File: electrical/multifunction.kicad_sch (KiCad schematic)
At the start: 23 parts

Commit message: Interim check-in
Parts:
- removed AVIONICS_CTL_SW, CABIN_CTL_SW, PANEL_CTL_SW: ~, symbol Switch:SW_SPST
- removed SMOKE_SW: SW_Push, symbol Switch:SW_Push
- added CWS_SW, PILOT_PTT: SW_Push, symbol Switch:SW_Push
- added PITCH_SW: SW_SPDT, symbol flyerx:SW_SPDT
- added SMKP, SMKP2: DT2P, symbol Connector:Conn_01x02_Socket
- added SMKR, SMKR2: DT2R, symbol Connector:Conn_01x02_Pin
- added SMOKE_SW: ~, symbol Switch:SW_SPST
- added STKP: DTM8P, symbol Connector:Conn_01x08_Socket
- added STKR: DTM8R, symbol Connector:Conn_01x08_Pin
- renumbered LANDING_LT to LEFT_LT, TAXI_LT to RIGHT_LT
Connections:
- net CAN_HI_IN: now also PILOT_PTT.1, STKP.8 (Pin_8), STKR.8 (Pin_8)
- net GND: now also PITCH_SW.2 (B), STKR.1 (Pin_1); no longer FLAPS_DN_SW.2, FLAPS_UP_SW.2, LEFT_LT.2, LEVEL_SW.2, RIGHT_LT.2
- net LIGHTING_12V: now also AVIONICS_CTL_POT.1, CABIN_CTL_POT.1, PANEL_CTL_POT.1
- net FUEL_PUMP_ON: now reaches GAD27.P271_10 (DISCRETE_IN_2)
- net FUEL_PUMP_ON: no longer GAD27.P271_28 (PILOT_ROLL_TRIM_L)
- net SMOKE_LT_ON: now reaches GAD27.P271_11 (DISCRETE_IN_3)
- net SMOKE_LT_ON: now also SMOKE_LT_FS.2, STKR.5 (Pin_5)
- net Orange: now reaches FLAPS_UP_SW.1
- net Orange: now also STKP.2 (Pin_2); no longer GAD27.P271_18 (FLAP_UP_1_SWITCH/ABS_FLAP_POSITION_1)
- net Grey: now reaches FLAPS_DN_SW.1
- net Grey: now also STKP.3 (Pin_3); no longer GAD27.P271_19 (FLAP_DOWN_1_SWITCH/ABS_FLAP_POSITION_2)
- net at GAD27.P271_24 (PILOT_PITCH_TRIM_UP): now also PITCH_SW.3 (C)
- net at GAD27.P271_25 (PILOT_PITCH_TRIM_DN): now also PITCH_SW.1 (A)
- net Purple: now reaches LEVEL_SW.1
- net Purple: now also STKP.6 (Pin_6); no longer GAD27.P271_9 (DISCRETE_IN_1)
- net PITCH_TRIM_PWR: now reaches GAD27.P272_1 (PITCH_TRIM_POWER_IN)
- net PITCH_TRIM1: now reaches GAD27.P272_11 (PITCH_TRIM_OUT_1)
- net PITCH_TRIM2: now reaches GAD27.P272_12 (PITCH_TRIM_OUT_2)
- net at GAD27.P272_9 (ROLL_TRIM_OUT_1), SMOKE_LT_FS.1: now also SMKR.1 (Pin_1); no longer SMOKE.1 (+)
- net at GAD27.TB_7 (FLAP_POWER_OUT_1): now also SMKR2.1 (Pin_1); no longer FLAPS.1 (+)
- net at GAD27.TB_8 (FLAP_POWER_OUT_2): now also SMKR2.2 (Pin_2); no longer FLAPS.2 (-)
- net Brown: now reaches SMOKE_LT.1
- net Brown: now also STKP.5 (Pin_5); no longer SMOKE_LT_FS.2
- new net: GAD27.P272_10 (ROLL_TRIM_OUT_2), SMKR.2 (Pin_2)
- new net: FLAPS.1 (+), SMKP2.1 (Pin_1)
- new net: FLAPS.2 (-), SMKP2.2 (Pin_2)
- new net: SMKP.1 (Pin_1), SMOKE.1 (+)
- new net: SMKP.2 (Pin_2), SMOKE.2 (-)
- new net Black: CWS_SW.2, FLAPS_DN_SW.2, FLAPS_UP_SW.2, LEVEL_SW.2, PILOT_PTT.2, SMOKE_LT.2, SMOKE_SW.2 (B), STKP.1 (Pin_1)
- new net CWS_ON: STKR.7 (Pin_7)
- new net Earth: LEFT_LT.2, RIGHT_LT.2
- new net Pink: SMOKE_SW.1 (A), STKP.4 (Pin_4)
- new net Red: CWS_SW.1, STKP.7 (Pin_7)
- new net White/Green: GAD27.P271_28 (PILOT_ROLL_TRIM_L), STKR.4 (Pin_4)
- new net White/Grey: GAD27.P271_19 (FLAP_DOWN_1_SWITCH/ABS_FLAP_POSITION_2), STKR.3 (Pin_3)
- new net White/Orange: GAD27.P271_18 (FLAP_UP_1_SWITCH/ABS_FLAP_POSITION_1), STKR.2 (Pin_2)
- new net White/Purple: GAD27.P271_9 (DISCRETE_IN_1), STKR.6 (Pin_6)
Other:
- moved on the sheet: AVIONICS_CTL_POT, CABIN_CTL_POT, FLAPS, FLAPS_DN_SW, FLAPS_UP_SW, LANDING_SW, LEVEL_SW, PANEL_CTL_POT, SMOKE, SMOKE_LT, TAXI_SW, WAG_SW

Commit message: Updated from learnings from N78HR
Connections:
- net FUEL_PUMP_ON is gone; now on net SMOKE_LT_ON: GAD27.P271_10 (DISCRETE_IN_2)
- net SMOKE_LT_ON: no longer GAD27.P271_11 (DISCRETE_IN_3)
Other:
- note added: "Not sure if using the Roll Trim will work for smoke"

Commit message: Interim check-in
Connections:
- net PITCH_TRIM1 is gone; now on net CAN_HI_IN: GAD27.P272_11 (PITCH_TRIM_OUT_1)
- net PITCH_TRIM2 is gone; now on net CAN_LO_IN: GAD27.P272_12 (PITCH_TRIM_OUT_2)
- net CAN_HI_IN: now also GAD27.P272_9 (ROLL_TRIM_OUT_1), GAD27.TB_7 (FLAP_POWER_OUT_1), SMKR.1 (Pin_1), SMKR2.1 (Pin_1), SMOKE_LT_FS.1
- net CAN_LO_IN: now also GAD27.P272_10 (ROLL_TRIM_OUT_2), GAD27.TB_8 (FLAP_POWER_OUT_2), SMKR.2 (Pin_2), SMKR2.2 (Pin_2)
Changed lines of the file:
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@@
 	(wire
 		(pts
+			(xy 83.82 175.26) (xy 97.79 175.26)
+		)
+		(stroke
+			(width 0)
+			(type dash)
+		)
+	)
+	(wire
+		(pts
 			(xy 81.28 74.93) (xy 100.33 74.93)
 		)
@@
 		)
 	)
+	(label "White"
+		(at 81.28 217.17 0)
+		(effects
+			(font
+				(size 1.27 1.27)
+			)
+			(justify left bottom)
+		)
+	)
 	(label "White{slash}Yellow"
 		(at 134.62 71.12 180)
@@
 		)
 	)
+	(label "White"
+		(at 81.28 177.8 0)
+		(effects
+			(font
+				(size 1.27 1.27)
+			)
+			(justify left bottom)
+		)
+	)
 	(label "Grey"
 		(at 144.78 66.04 0)
@@
 		)
 	)
+	(label "White{slash}Blue"
+		(at 81.28 180.34 0)
+		(effects
+			(font
+				(size 1.27 1.27)
+			)
+			(justify left bottom)
+		)
+	)
 	(label "White{slash}Black"
 		(at 134.62 60.96 180)
@@
 		)
 	)
+	(label "White{slash}Blue"
+		(at 111.76 185.42 180)
+		(effects
+			(font
+				(size 1.27 1.27)
+			)
+			(justify right bottom)
+		)
+	)
+	(label "White"
+		(at 111.76 182.88 180)
+		(effects
+			(font
+				(size 1.27 1.27)
+			)
+			(justify right bottom)
+		)
+	)
+	(label "White"
+		(at 81.28 182.88 0)
+		(effects
+			(font
+				(size 1.27 1.27)
+			)
+			(justify left bottom)
+		)
+	)
+	(label "White"
+		(at 116.84 217.17 180)
+		(effects
+			(font
+				(size 1.27 1.27)
+			)
+			(justify right bottom)
+		)
+	)
 	(label "White{slash}Purple"
 		(at 134.62 73.66 180)
@@
 	)
 	(label "White{slash}Blue"
+		(at 81.28 219.71 0)
+		(effects
+			(font
+				(size 1.27 1.27)
+			)
+			(justify left bottom)
+		)
+	)
+	(label "White{slash}Blue"
+		(at 81.28 185.42 0)
+		(effects
+			(font
+				(size 1.27 1.27)
+			)
+			(justify left bottom)
+		)
+	)
+	(label "White{slash}Blue"
+		(at 116.84 219.71 180)
+		(effects
+			(font
+				(size 1.27 1.27)
+			)
+			(justify right bottom)
+		)
+	)
+	(label "White{slash}Blue"
 		(at 81.28 35.56 0)
 		(effects
@@
 		(dnp no)
 		(property "Reference" "LEFT_LT"
-			(at 91.44 210.82 0)
+			(at 116.078 211.582 0)
 			(effects
 				(font
@@
 		(dnp no)
 		(property "Reference" "RIGHT_LT"
-			(at 91.44 213.36 0)
+			(at 116.586 213.868 0)
 			(effects
 				(font
@@
 					(unit 1)
 				)
+			)
+		)
+	)
+	(symbol
+		(lib_id "power:GNDS")
+		(at 83.82 175.26 270)
+		(unit 1)
+		(exclude_from_sim no)
+		(in_bom yes)
+		(on_board yes)
+		(dnp no)
+		(fields_autoplaced yes)
+		(property "Reference" "#PWR053"
+			(at 77.47 175.26 0)
+			(effects
+				(font
+					(size 1.27 1.27)
+				)
+				(hide yes)
+			)
+		)
+		(property "Value" "GNDS"
+			(at 78.74 175.26 0)
+			(effects
+				(font
+					(size 1.27 1.27)
+				)
+				(hide yes)
+			)
+		)
+		(property "Footprint" ""
+			(at 83.82 175.26 0)
+			(effects
+				(font
+					(size 1.27 1.27)
+				)
+				(hide yes)
+			)
+		)
+		(property "Datasheet" ""
+			(at 83.82 175.26 0)
+			(effects
+				(font
+					(size 1.27 1.27)
+				)
+				(hide yes)
+			)
+		)
+		(property "Description" "Power symbol creates a global label with name \"GNDS\" , signal ground"
+			(at 83.82 175.26 0)
+			(effects
+				(font
+					(size 1.27 1.27)
+				)
+				(hide yes)
+			)
+		)
+		(pin "1"
+		)
+		(instances
+			(project "electrical"
+				(path "/e8ec215a-dbe2-4eba-a577-e50a0a128049/67540fe5-9b6d-4d8c-9d03-cde1487f48ae"
+					(reference "#PWR053")
+					(unit 1)
+				)

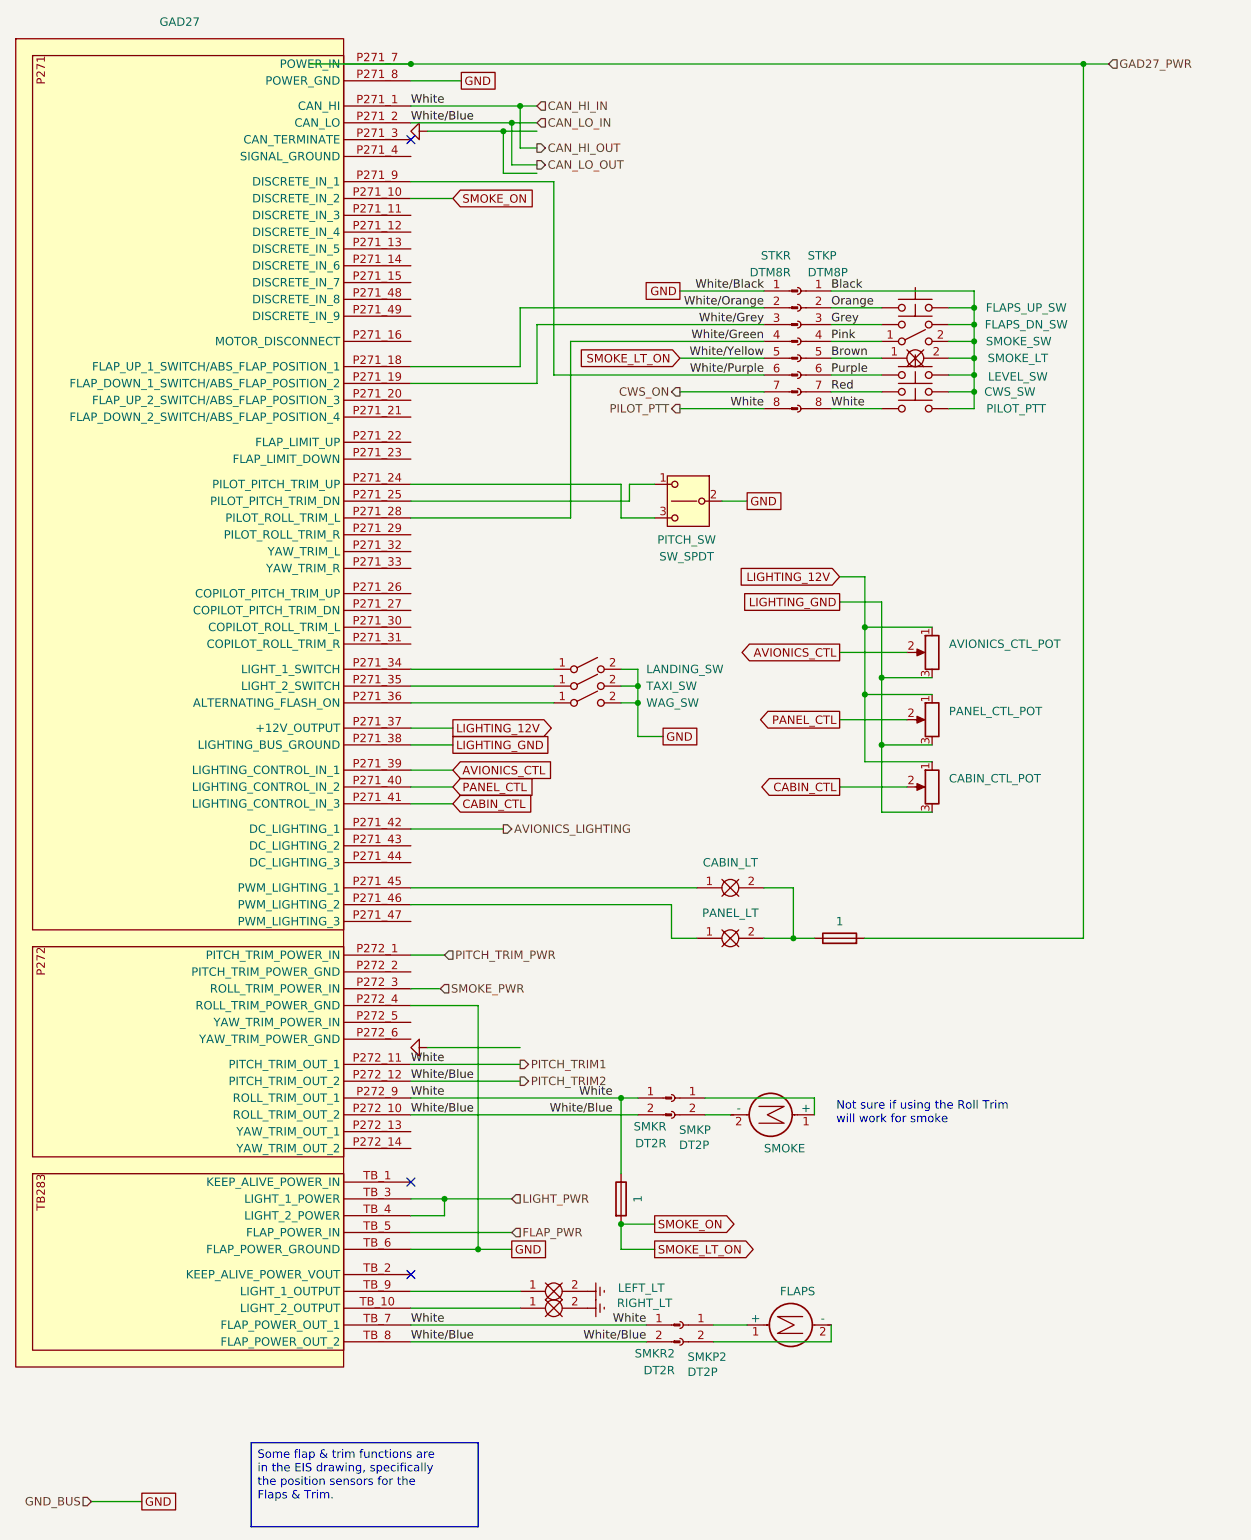
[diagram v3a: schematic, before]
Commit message: Went through and changed a lot from discussions and tradeoffs. Added GTX 330, rmemoved Connext from GDU and added to GPS 175 from GDL 52. Added relay for smoke and to not use GAD 27. Added Tach sensor for SureFly. Added carb heat. Added connectors to run panel disconnected.
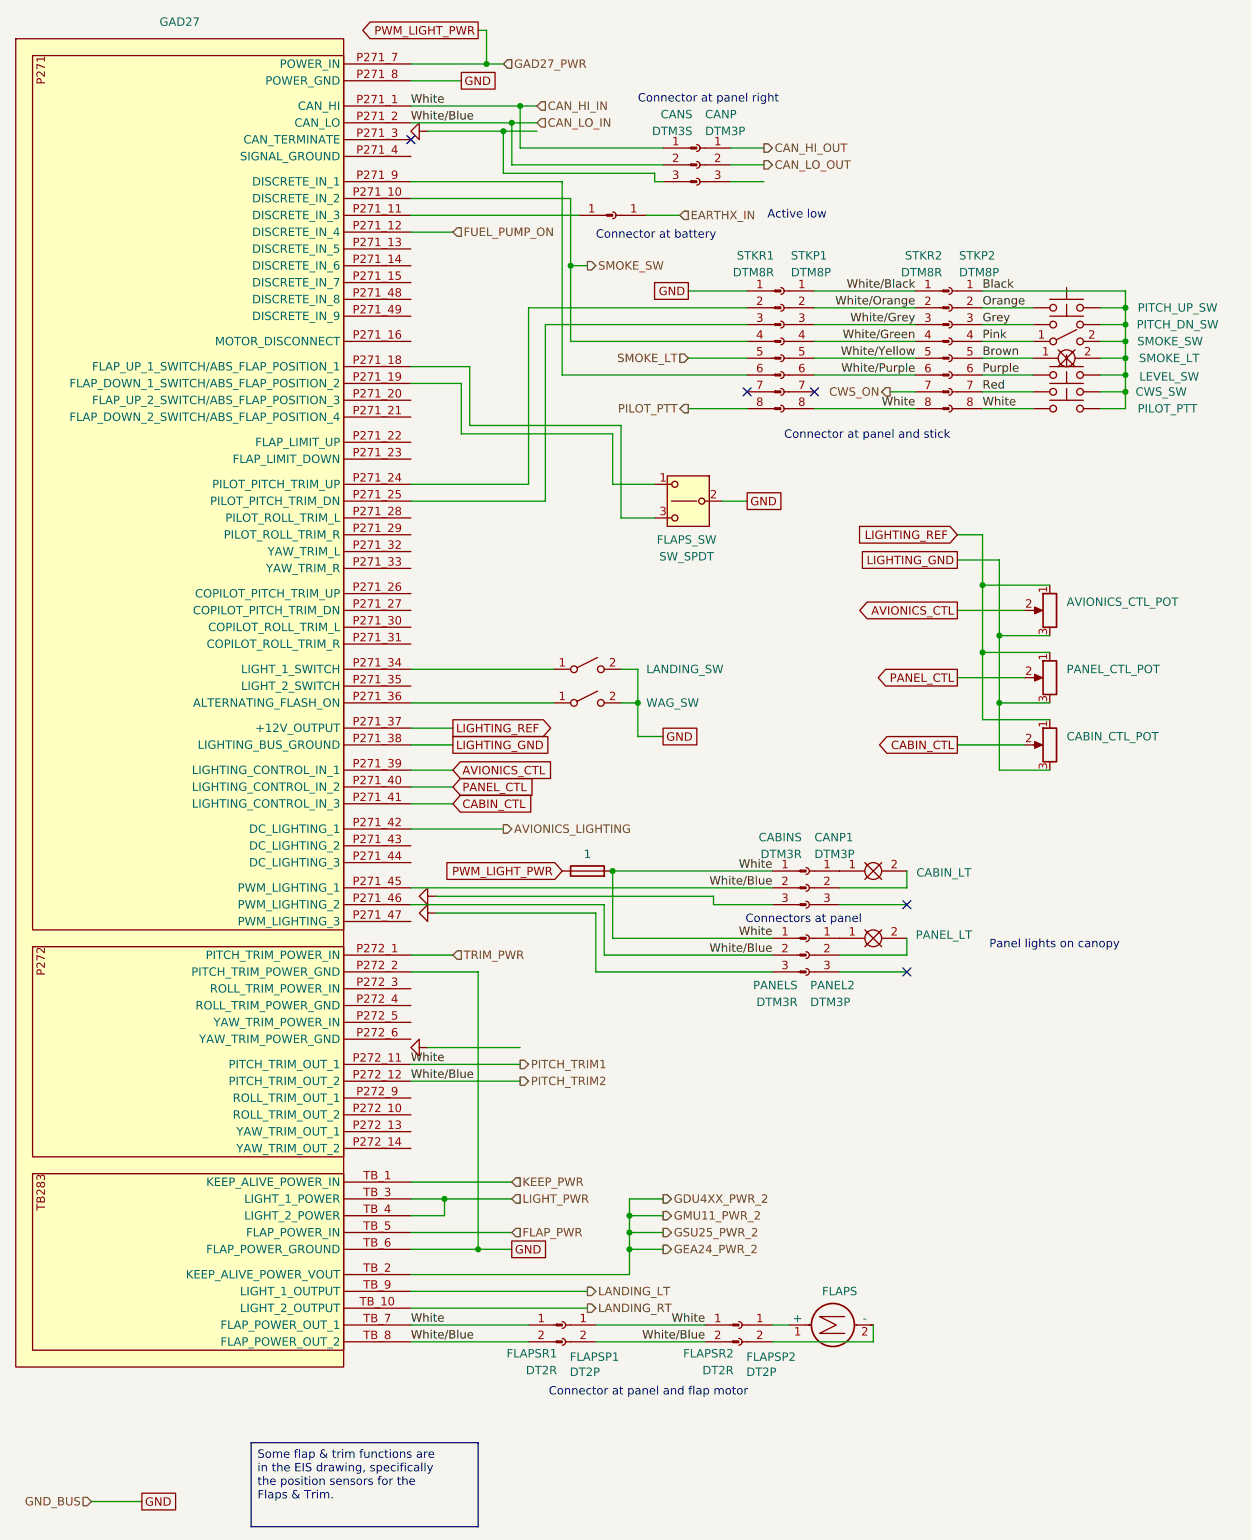
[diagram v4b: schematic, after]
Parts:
- removed LEFT_LT, RIGHT_LT: ~, symbol flyerx:Bulb
- removed SMKP: DT2P, symbol Connector:Conn_01x02_Socket
- removed SMKR: DT2R, symbol Connector:Conn_01x02_Pin
- removed SMOKE: Motor_DC, symbol Motor:Motor_DC
- removed SMOKE_LT_FS: 1, symbol Device:Fuse
- removed TAXI_SW: ~, symbol Switch:SW_SPST
- added CABINS, PANELS: DTM3R, symbol Connector:Conn_01x03_Pin
- added CANP, CANP1, PANEL2: DTM3P, symbol Connector:Conn_01x03_Socket
- added CANS: DTM3S, symbol Connector:Conn_01x03_Pin
- added EARTHXP: Conn_01x01_Pin, symbol Connector:Conn_01x01_Pin
- added EARTHXS: Conn_01x01_Socket, symbol Connector:Conn_01x01_Socket
- added FLAPSP1: DT2P, symbol Connector:Conn_01x02_Socket
- added FLAPSR1: DT2R, symbol Connector:Conn_01x02_Pin
- added STKP1: DTM8P, symbol Connector:Conn_01x08_Socket
- added STKR1: DTM8R, symbol Connector:Conn_01x08_Pin
- renumbered SMKP2 to FLAPSP2, SMKR2 to FLAPSR2, PITCH_SW to FLAPS_SW, FLAPS_DN_SW to PITCH_DN_SW, FLAPS_UP_SW to PITCH_UP_SW, STKP to STKP2, STKR to STKR2
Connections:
- net CAN_HI_IN: now also PANEL_LT_FS.2, CABINS.1 (Pin_1), CANS.1 (Pin_1), FLAPSP1.1 (Pin_1), FLAPSR1.1 (Pin_1), PANELS.1 (Pin_1), STKP1.8 (Pin_8); no longer GAD27.P272_9 (ROLL_TRIM_OUT_1)
- net CAN_LO_IN: now also GAD27.P271_45 (PWM_LIGHTING_1), GAD27.P271_46 (PWM_LIGHTING_2), CABINS.2 (Pin_2), CANS.2 (Pin_2), FLAPSP1.2 (Pin_2), FLAPSR1.2 (Pin_2), PANELS.2 (Pin_2); no longer GAD27.P272_10 (ROLL_TRIM_OUT_2)
- net GND: now also GAD27.P272_2 (PITCH_TRIM_POWER_GND), STKR1.1 (Pin_1); no longer GAD27.P272_4 (ROLL_TRIM_POWER_GND), STKR2.1 (Pin_1)
- net GNDS: now also CABINS.3 (Pin_3), CANS.3 (Pin_3), PANELS.3 (Pin_3)
- net White/Green: now also STKP1.4 (Pin_4); no longer GAD27.P271_28 (PILOT_ROLL_TRIM_L)
- net White/Grey: now also STKP1.3 (Pin_3); no longer GAD27.P271_19 (FLAP_DOWN_1_SWITCH/ABS_FLAP_POSITION_2)
- net White/Orange: now also STKP1.2 (Pin_2); no longer GAD27.P271_18 (FLAP_UP_1_SWITCH/ABS_FLAP_POSITION_1)
- net White/Purple: now also STKP1.6 (Pin_6); no longer GAD27.P271_9 (DISCRETE_IN_1)
- net at GAD27.P271_11 (DISCRETE_IN_3): now also EARTHXP.1 (Pin_1)
- net FUEL_PUMP_ON: now reaches GAD27.P271_12 (DISCRETE_IN_4)
- net at FLAPS_SW.3 (C): now also GAD27.P271_18 (FLAP_UP_1_SWITCH/ABS_FLAP_POSITION_1); no longer GAD27.P271_24 (PILOT_PITCH_TRIM_UP)
- net at FLAPS_SW.1 (A): now also GAD27.P271_19 (FLAP_DOWN_1_SWITCH/ABS_FLAP_POSITION_2); no longer GAD27.P271_25 (PILOT_PITCH_TRIM_DN)
- net at CABIN_LT.1: now also CANP1.1 (Pin_1); no longer GAD27.P271_45 (PWM_LIGHTING_1)
- net at PANEL_LT.1: now also PANEL2.1 (Pin_1); no longer GAD27.P271_46 (PWM_LIGHTING_2)
- net KEEP_PWR: now reaches GAD27.TB_1 (KEEP_ALIVE_POWER_IN)
- net LANDING_RT: now reaches GAD27.TB_10 (LIGHT_2_OUTPUT)
- net GDU4XX_PWR_2: now reaches GAD27.TB_2 (KEEP_ALIVE_POWER_VOUT)
- net LANDING_LT: now reaches GAD27.TB_9 (LIGHT_1_OUTPUT)
- net GAD27_PWR renamed PWM_LIGHT_PWR
- net PWM_LIGHT_PWR: now also PANEL_LT_FS.1; no longer PANEL_LT_FS.2
- net LIGHTING_12V renamed LIGHTING_REF
- net PITCH_TRIM_PWR renamed TRIM_PWR
- net SMOKE_LT_ON renamed SMOKE_SW
- net SMOKE_SW: now also STKR1.4 (Pin_4); no longer STKR2.5 (Pin_5)
- net SMOKE_PWR: no longer names the net of GAD27.P272_3 (ROLL_TRIM_POWER_IN)
- new net: GAD27.P271_24 (PILOT_PITCH_TRIM_UP), STKR1.2 (Pin_2)
- new net: GAD27.P271_25 (PILOT_PITCH_TRIM_DN), STKR1.3 (Pin_3)
- new net: GAD27.P271_9 (DISCRETE_IN_1), STKR1.6 (Pin_6)
- new net: PANEL2.2 (Pin_2), PANEL_LT.2
- new net: CABIN_LT.2, CANP1.2 (Pin_2)
- new net CAN_HI_OUT: CANP.1 (Pin_1)
- new net CAN_LO_OUT: CANP.2 (Pin_2)
- new net EARTHX_IN: EARTHXS.1 (Pin_1)
- new net PILOT_PTT: STKR1.8 (Pin_8)
- new net SMOKE_LT: STKR1.5 (Pin_5)
- new net White/Black: STKP1.1 (Pin_1), STKR2.1 (Pin_1)
- new net White/Yellow: STKP1.5 (Pin_5), STKR2.5 (Pin_5)
- no-connect marks 3 -> 5
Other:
- note added: "Active low"
- note added: "Connector at battery"
- note added: "Connector at panel and flap motor"
- note added: "Connector at panel and stick"
- note added: "Connector at panel right"
- note added: "Connectors at panel"
- note added: "Panel lights on canopy"
- note removed: "Not sure if using the Roll Trim will work for smoke"
- moved on the sheet: AVIONICS_CTL_POT, CABIN_CTL_POT, CABIN_LT, CWS_SW, FLAPS, FLAPSP2, FLAPSR2, LEVEL_SW, PANEL_CTL_POT, PANEL_LT, PILOT_PTT, PITCH_DN_SW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
